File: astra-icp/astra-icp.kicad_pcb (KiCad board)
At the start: 2 copper layers, 127.5 x 97.5 mm, 45 parts, among them J1 Conn_02x05_Top_Bottom

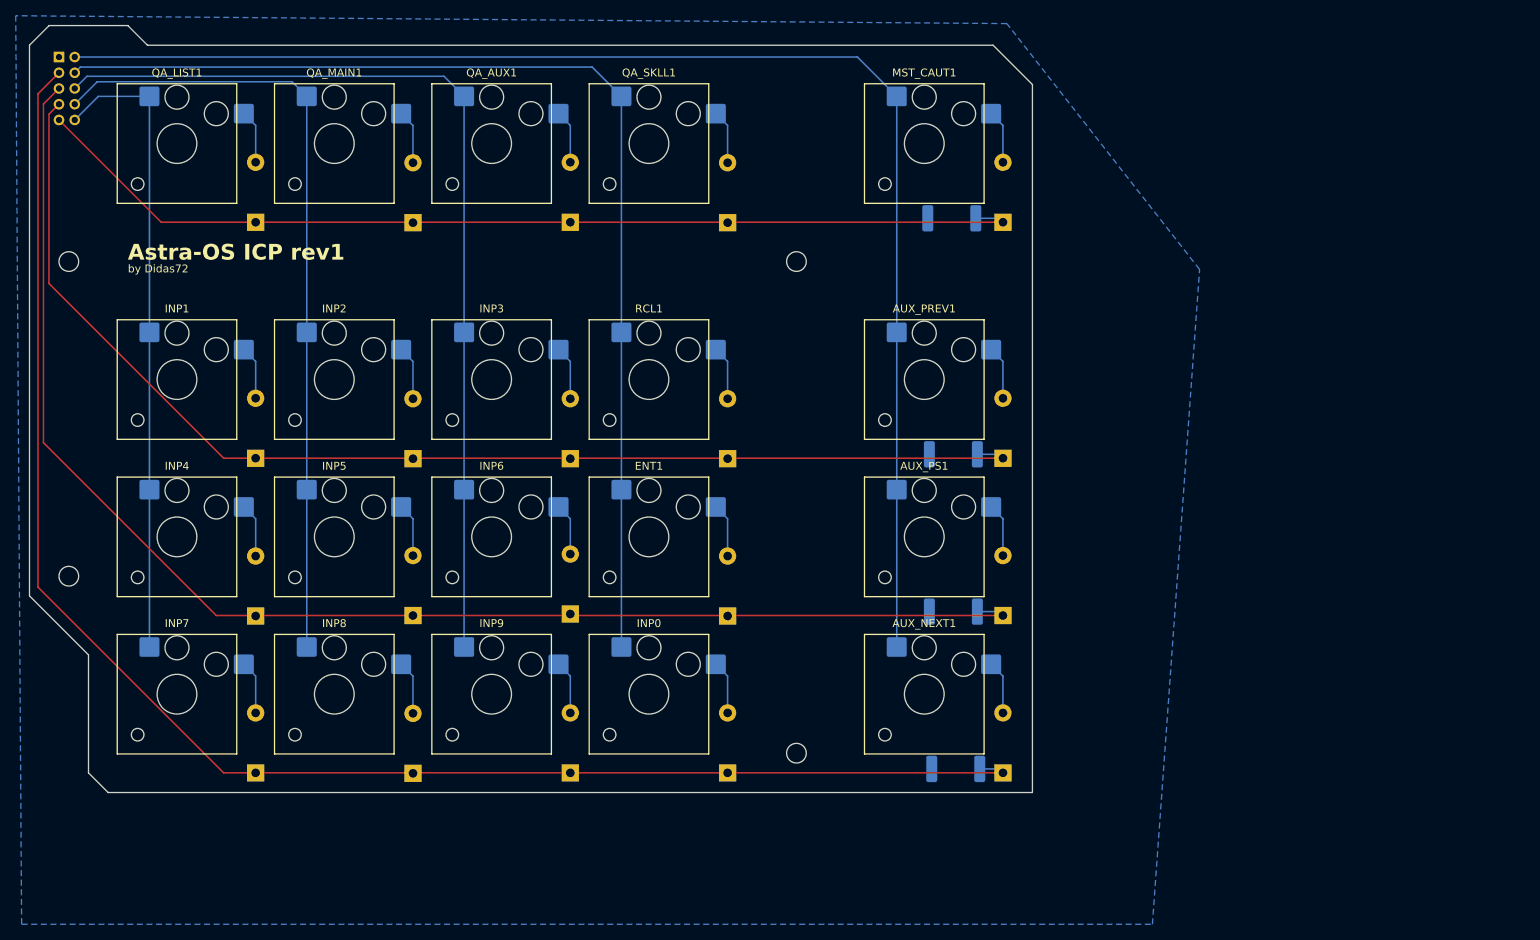
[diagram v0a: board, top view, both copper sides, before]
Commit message: feat: Schematic and partial PCB for ICP rev2
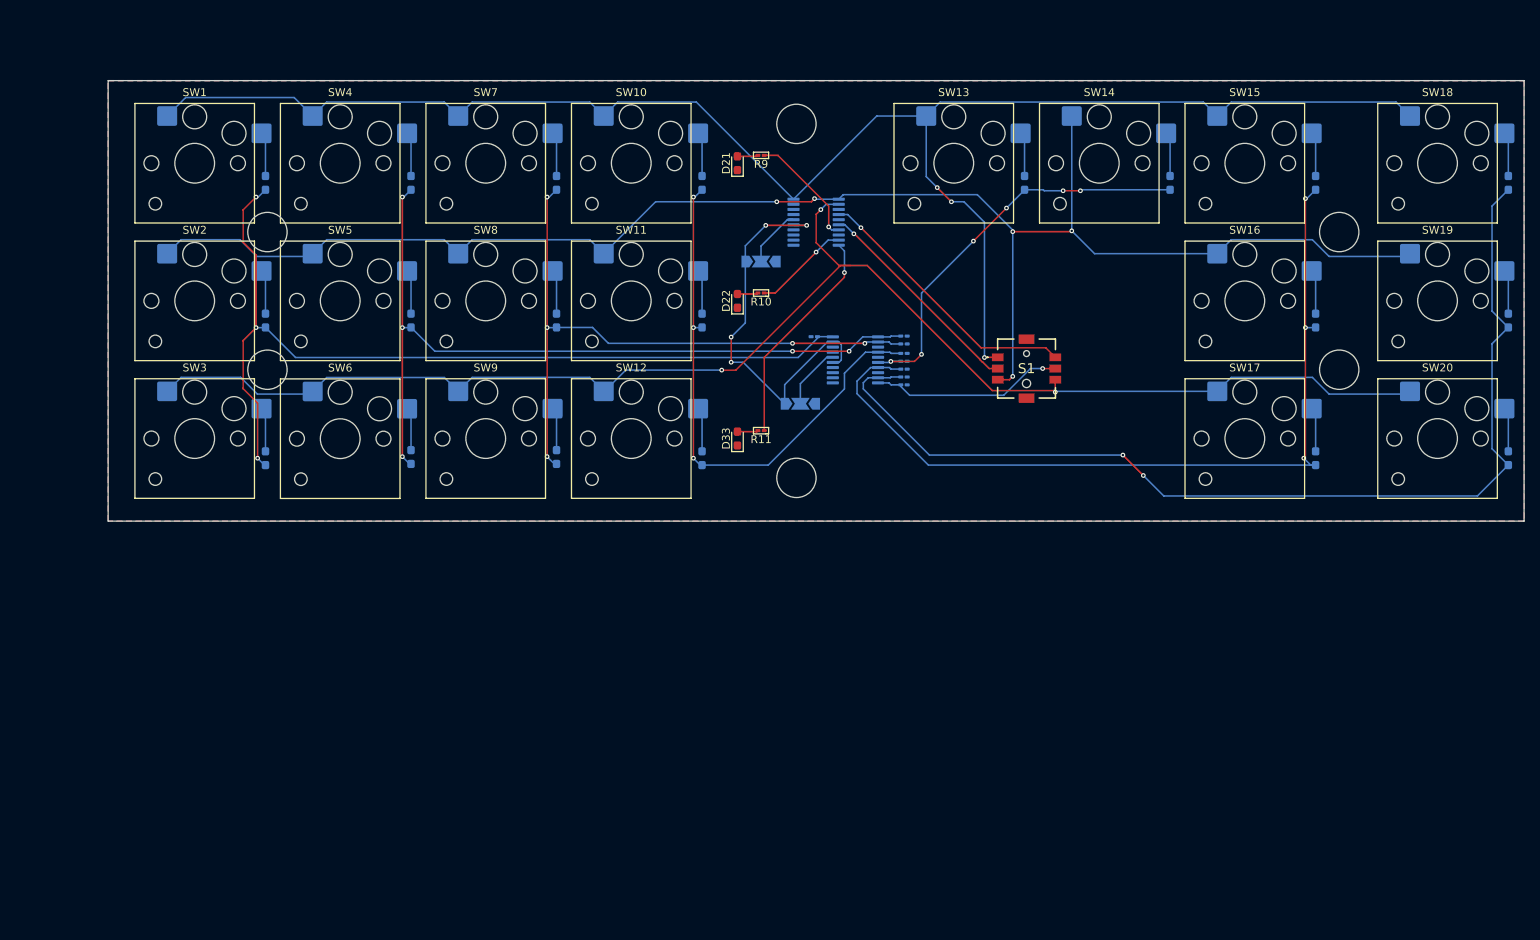
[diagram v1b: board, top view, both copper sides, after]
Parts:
- removed AUX_NEXT1, AUX_PREV1, AUX_PS1, ENT1, INP0, INP1, INP2, INP3, INP4, INP5, INP6, INP7, INP8, INP9, MST_CAUT1, QA_AUX1, QA_LIST1, QA_MAIN1, QA_SKLL1, RCL1: SW_Push_Dual, PCM_Switch_Keyboard_Hotswap_Kailh:SW_Hotswap_Kailh_Choc_V2_1.00u
- removed J1: Conn_02x05_Top_Bottom, Connector_PinSocket_2.00mm:PinSocket_2x05_P2.00mm_Vertical
- added D21: 599-2000-147F, LED_SMD:LED_0603_1608Metric_Pad1.05x0.95mm_HandSolder, F.Cu at (105.0, 32.5)
- added D22: 599-2000-147F, LED_SMD:LED_0603_1608Metric_Pad1.05x0.95mm_HandSolder, F.Cu at (105.0, 50.0)
- added D33: 599-2000-147F, LED_SMD:LED_0603_1608Metric_Pad1.05x0.95mm_HandSolder, F.Cu at (105.0, 67.5)
- added JP1: SolderJumper, Jumper:SolderJumper-3_P2.0mm_Open_TrianglePad1.0x1.5mm, B.Cu at (113.0, 63.1)
- added JP2: SolderJumper, Jumper:SolderJumper-3_P2.0mm_Open_TrianglePad1.0x1.5mm, B.Cu at (108.0, 45.0)
- added R10: 15, PCM_Resistor_SMD_AKL:R_0201_0603Metric_Pad0.64x0.40mm_HandSolder, F.Cu at (108.0, 49.0)
- added R11: 15, PCM_Resistor_SMD_AKL:R_0201_0603Metric_Pad0.64x0.40mm_HandSolder, F.Cu at (108.0, 66.5)
- added R5: 47k, PCM_Resistor_SMD_AKL:R_0201_0603Metric_Pad0.64x0.40mm_HandSolder, B.Cu at (126.2, 57.7)
- added R6: 47k, PCM_Resistor_SMD_AKL:R_0201_0603Metric_Pad0.64x0.40mm_HandSolder, B.Cu at (126.2, 58.7)
- added R7: 47k, PCM_Resistor_SMD_AKL:R_0201_0603Metric_Pad0.64x0.40mm_HandSolder, B.Cu at (126.2, 59.7)
- added R8: 47k, PCM_Resistor_SMD_AKL:R_0201_0603Metric_Pad0.64x0.40mm_HandSolder, B.Cu at (126.2, 60.7)
- added R9: 15, PCM_Resistor_SMD_AKL:R_0201_0603Metric_Pad0.64x0.40mm_HandSolder, F.Cu at (108.0, 31.5)
- added S1: MU-BUE70R, footprints:MUBUE70R, F.Cu at (141.8, 58.6)
- added SW1: CHOC_HS, PCM_Switch_Keyboard_Hotswap_Kailh:SW_Hotswap_Kailh_Choc_V1V2_1.00u, F.Cu at (36.0, 32.5)
- added SW10: CHOC_HS, PCM_Switch_Keyboard_Hotswap_Kailh:SW_Hotswap_Kailh_Choc_V1V2_1.00u, F.Cu at (91.5, 32.5)
- added SW11: CHOC_HS, PCM_Switch_Keyboard_Hotswap_Kailh:SW_Hotswap_Kailh_Choc_V1V2_1.00u, F.Cu at (91.5, 50.0)
- added SW12: CHOC_HS, PCM_Switch_Keyboard_Hotswap_Kailh:SW_Hotswap_Kailh_Choc_V1V2_1.00u, F.Cu at (91.5, 67.5)
- added SW13: CHOC_HS, PCM_Switch_Keyboard_Hotswap_Kailh:SW_Hotswap_Kailh_Choc_V1V2_1.00u, F.Cu at (132.5, 32.5)
- added SW14: CHOC_HS, PCM_Switch_Keyboard_Hotswap_Kailh:SW_Hotswap_Kailh_Choc_V1V2_1.00u, F.Cu at (151.0, 32.5)
- added SW15: CHOC_HS, PCM_Switch_Keyboard_Hotswap_Kailh:SW_Hotswap_Kailh_Choc_V1V2_1.00u, F.Cu at (169.5, 32.5)
- added SW16: CHOC_HS, PCM_Switch_Keyboard_Hotswap_Kailh:SW_Hotswap_Kailh_Choc_V1V2_1.00u, F.Cu at (169.5, 50.0)
- added SW17: CHOC_HS, PCM_Switch_Keyboard_Hotswap_Kailh:SW_Hotswap_Kailh_Choc_V1V2_1.00u, F.Cu at (169.5, 67.5)
- added SW18: CHOC_HS, PCM_Switch_Keyboard_Hotswap_Kailh:SW_Hotswap_Kailh_Choc_V1V2_1.00u, F.Cu at (194.0, 32.5)
- added SW19: CHOC_HS, PCM_Switch_Keyboard_Hotswap_Kailh:SW_Hotswap_Kailh_Choc_V1V2_1.00u, F.Cu at (194.0, 50.0)
- added SW2: CHOC_HS, PCM_Switch_Keyboard_Hotswap_Kailh:SW_Hotswap_Kailh_Choc_V1V2_1.00u, F.Cu at (36.0, 50.0)
- added SW20: CHOC_HS, PCM_Switch_Keyboard_Hotswap_Kailh:SW_Hotswap_Kailh_Choc_V1V2_1.00u, F.Cu at (194.0, 67.5)
- added SW3: CHOC_HS, PCM_Switch_Keyboard_Hotswap_Kailh:SW_Hotswap_Kailh_Choc_V1V2_1.00u, F.Cu at (36.0, 67.5)
- added SW4: CHOC_HS, PCM_Switch_Keyboard_Hotswap_Kailh:SW_Hotswap_Kailh_Choc_V1V2_1.00u, F.Cu at (54.5, 32.5)
- added SW5: CHOC_HS, PCM_Switch_Keyboard_Hotswap_Kailh:SW_Hotswap_Kailh_Choc_V1V2_1.00u, F.Cu at (54.5, 50.0)
- added SW6: CHOC_HS, PCM_Switch_Keyboard_Hotswap_Kailh:SW_Hotswap_Kailh_Choc_V1V2_1.00u, F.Cu at (54.5, 67.5)
- added SW7: CHOC_HS, PCM_Switch_Keyboard_Hotswap_Kailh:SW_Hotswap_Kailh_Choc_V1V2_1.00u, F.Cu at (73.0, 32.5)
- added SW8: CHOC_HS, PCM_Switch_Keyboard_Hotswap_Kailh:SW_Hotswap_Kailh_Choc_V1V2_1.00u, F.Cu at (73.0, 50.0)
- added SW9: CHOC_HS, PCM_Switch_Keyboard_Hotswap_Kailh:SW_Hotswap_Kailh_Choc_V1V2_1.00u, F.Cu at (73.0, 67.5)
- added U1: PCF8574ATS, Package_SO:SSOP-20_4.4x6.5mm_P0.65mm, B.Cu at (115.0, 40.0)
- added U2: PCF8574ATS, Package_SO:SSOP-20_4.4x6.5mm_P0.65mm, B.Cu at (120.0, 57.5)
- D1, D10, D11, D12, D13, D14, D15, D16, D17, D18, D19, D2, D20, D3, D4, D5, D6, D7, D8, D9: value 1N5400 -> D; footprint Diode_THT:D_DO-41_SOD81_P7.62mm_Horizontal -> PCM_Diode_SMD_AKL:D_0603_1608Metric_Pad1.05x0.95mm_HandSolder
- R1, R2, R3, R4: footprint Resistor_SMD:R_2512_6332Metric_Pad1.40x3.35mm_HandSolder -> PCM_Resistor_SMD_AKL:R_0201_0603Metric_Pad0.64x0.40mm_HandSolder
- moved D15 120.8 mm to (178.5, 35.0)
- moved D13 95.2 mm to (141.5, 35.0)
- moved D16 94.3 mm to (178.5, 52.5)
- moved D14 93.9 mm to (160.0, 35.0)
- moved D11 80.8 mm to (100.5, 52.5)
- moved D10 79.1 mm to (100.5, 35.0)
- moved D17 77.4 mm to (178.5, 70.0)
- moved D5 76.3 mm to (63.5, 52.5)
- moved D20 75.7 mm to (203.0, 70.0)
- moved D19 74.4 mm to (203.0, 52.5)
- moved D18 73.2 mm to (203.0, 35.0)
- moved R1 57.8 mm to (114.8, 54.5)
- moved D12 54.4 mm to (100.5, 70.0)
- moved D3 49.0 mm to (45.0, 70.0)
- moved D4 40.6 mm to (63.5, 35.0)
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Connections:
- D1 pad 1: Net-(D1-K) -> COL0
- D10 pad 1: Net-(D10-K) -> COL3
- D11 pad 1: Net-(D11-K) -> COL3
- D12 pad 1: Net-(D11-K) -> COL3
- D13 pad 1: Net-(D10-K) -> COL4
- D14 pad 1: Net-(D10-K) -> COL4
- D15 pad 1: Net-(D11-K) -> COL5
- D16 pad 1: Net-(D11-K) -> COL5
- D17 pad 1: Net-(D10-K) -> COL5
- D18 pad 1: Net-(D18-K) -> COL6
- D19 pad 1: Net-(D10-K) -> COL6
- D2 pad 1: Net-(D1-K) -> COL0
- D20 pad 1: Net-(D11-K) -> COL6
- D3 pad 1: Net-(D1-K) -> COL0
- D4 pad 1: Net-(D1-K) -> COL1
- D5 pad 1: Net-(D1-K) -> COL1
- D6 pad 1: Net-(D18-K) -> COL1
- D7 pad 1: Net-(D18-K) -> COL2
- D8 pad 1: Net-(D18-K) -> COL2
- D9 pad 1: Net-(D18-K) -> COL2
- R1 pad 2: Net-(D11-K) -> COL0
- R2 pad 2: Net-(D10-K) -> COL1
- R3 pad 2: Net-(D18-K) -> COL2
- R4 pad 2: Net-(D1-K) -> COL3
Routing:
- net ROW0: track 0.00 -> 212.5 mm, vias 0 -> 3
- net ROW1: track 0.00 -> 206.0 mm, vias 0 -> 5
- net Net-(D11-K): track 202.1 -> 0.00 mm
- net ROW2: track 0.00 -> 192.0 mm, vias 0 -> 3
- net Net-(D10-K): track 180.4 -> 0.00 mm
- net Net-(J1-Pin_2): track 176.6 -> 0.00 mm
- net Net-(D18-K): track 157.3 -> 0.00 mm
- net Net-(J1-Pin_4): track 141.3 -> 0.00 mm
- net COL6: track 0.00 -> 133.6 mm, vias 0 -> 2
- net Net-(D1-K): track 129.0 -> 0.00 mm
- net Net-(J1-Pin_6): track 121.2 -> 0.00 mm
- net COL0: track 0.00 -> 115.1 mm, vias 0 -> 3
- net COL5: track 0.00 -> 108.5 mm, vias 0 -> 3
- net Net-(J1-Pin_8): track 101.4 -> 0.00 mm
- net COL1: track 0.00 -> 101.4 mm, vias 0 -> 5
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- added copper zone on F.Cu, net GND
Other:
- board size 127.5 x 97.5 mm -> 180 x 56 mm
- board text removed: "Astra-OS ICP rev1"
- board text removed: "by Didas72"

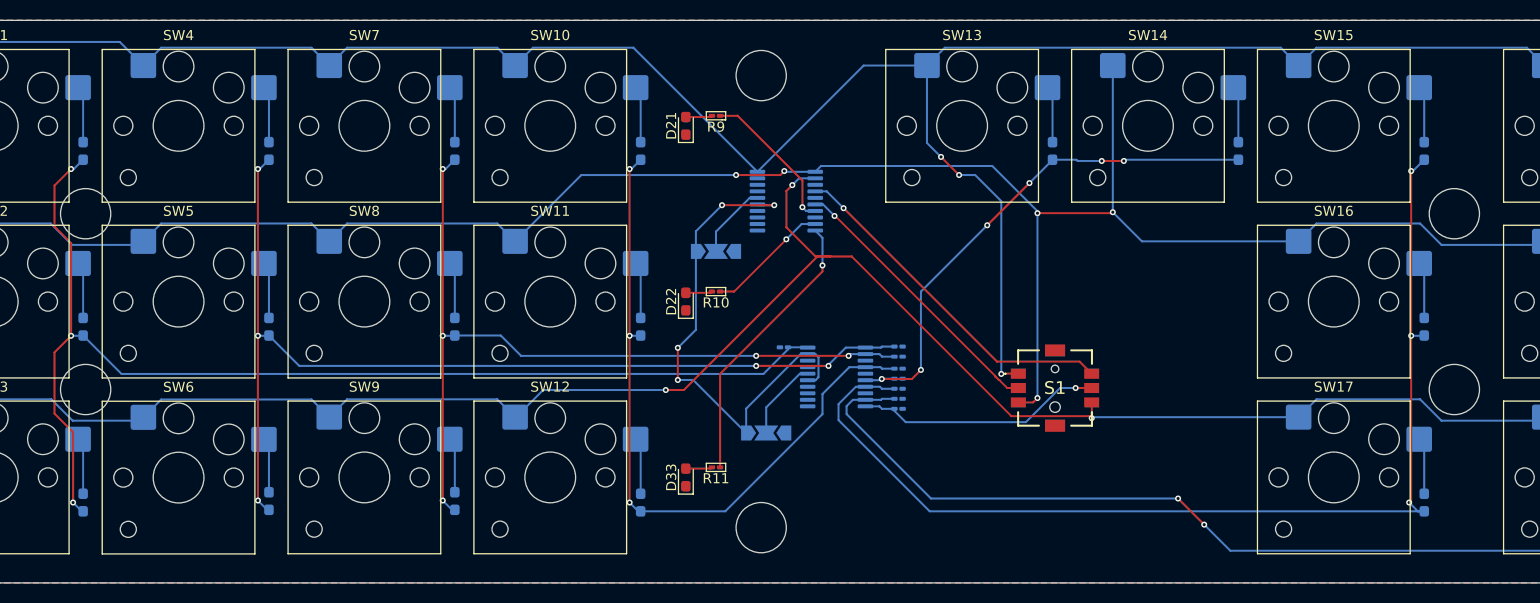
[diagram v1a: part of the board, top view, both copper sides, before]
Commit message: feat: Work on connectors and MCU-CAN signaling
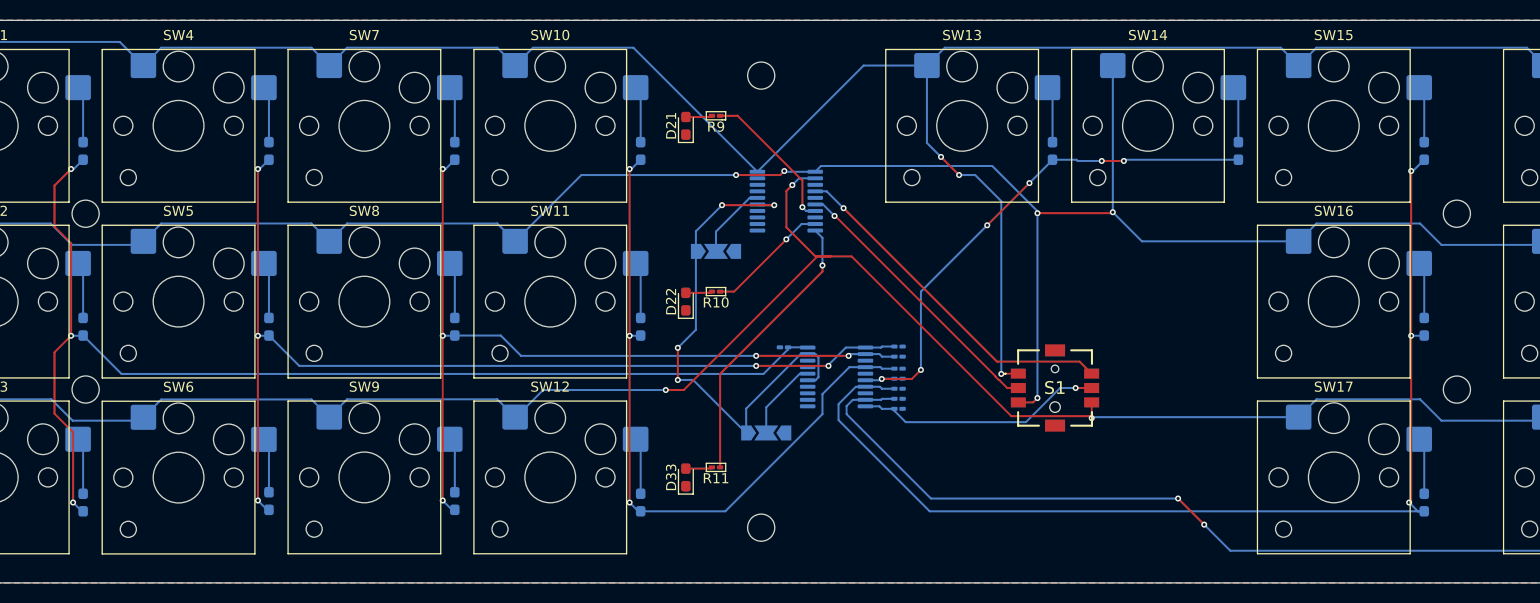
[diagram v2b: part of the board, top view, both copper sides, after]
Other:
- outline, holes or cut-outs redrawn
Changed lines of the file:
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@@
 	)
 	(gr_circle
-		(center 45.25 41.25)
-		(end 47.75 41.25)
-		(stroke
-			(width 0.05)
-			(type default)
-		)
-		(fill no)
-		(layer "Edge.Cuts")
-	)
-	(gr_circle
-		(center 181.5 41.25)
-		(end 184 41.25)
+		(center 181.752858 58.755315)
+		(end 183.102858 58.755315)
 		(stroke
 			(width 0.05)
@@
 	)
 	(gr_circle
-		(center 181.5 58.75)
-		(end 184 58.75)
+		(center 181.75 41.25)
+		(end 183.1 41.25)
+		(stroke
+			(width 0.05)
+			(type default)
+		)
+		(fill no)
+		(layer "Edge.Cuts")
+	)
+	(gr_circle
+		(center 112.5 72.5)
+		(end 113.85 72.5)
+		(stroke
+			(width 0.05)
+			(type default)
+		)
+		(fill no)
+		(layer "Edge.Cuts")
+	)
+	(gr_circle
+		(center 45.25 41.25)
+		(end 46.6 41.25)
+		(stroke
+			(width 0.05)
+			(type default)
+		)
+		(fill no)
+		(layer "Edge.Cuts")
+	)
+	(gr_circle
+		(center 45.25 58.75)
+		(end 46.6 58.75)
 		(stroke
 			(width 0.05)
@@
 	(gr_circle
 		(center 112.5 27.5)
-		(end 115 27.5)
+		(end 113.85 27.5)
 		(stroke
 			(width 0.05)
-			(type default)
-		)
-		(fill no)
-		(layer "Edge.Cuts")
-	)
-	(gr_circle
-		(center 112.5 72.5)
-		(end 115 72.5)
-		(stroke
-			(width 0.05)
-			(type default)
-		)
-		(fill no)
-		(layer "Edge.Cuts")
-	)
-	(gr_circle
-		(center 45.25 58.75)
-		(end 47.75 58.75)
-		(stroke
-			(width 0.05)

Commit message: feat: Mostly done ICP PCB
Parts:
- removed JP1, JP2: SolderJumper, Jumper:SolderJumper-3_P2.0mm_Open_TrianglePad1.0x1.5mm
- removed U1, U2: PCF8574ATS, Package_SO:SSOP-20_4.4x6.5mm_P0.65mm
- added C1: 100n, Capacitor_SMD:C_0603_1608Metric_Pad1.08x0.95mm_HandSolder, B.Cu at (124.5, 56.0)
- added C2: 100n, Capacitor_SMD:C_0603_1608Metric_Pad1.08x0.95mm_HandSolder, B.Cu at (127.5, 63.5)
- added C3: 100n, Capacitor_SMD:C_0603_1608Metric_Pad1.08x0.95mm_HandSolder, B.Cu at (119.8, 40.2)
- added C4: 100n, Capacitor_SMD:C_0603_1608Metric_Pad1.08x0.95mm_HandSolder, B.Cu at (111.2, 51.2)
- added C5: 4.7p, Capacitor_SMD:C_0603_1608Metric_Pad1.08x0.95mm_HandSolder, B.Cu at (110.8, 40.2)
- added D23: 5V_IND, LED_SMD:LED_0603_1608Metric_Pad1.05x0.95mm_HandSolder, B.Cu at (132.8, 71.0)
- added D24: 3V3_IND, LED_SMD:LED_0603_1608Metric_Pad1.05x0.95mm_HandSolder, B.Cu at (132.8, 72.8)
- added IC1: ATA6561-GAQW-N, footprints:SOIC127P600X175-8N, B.Cu at (123.0, 60.8)
- added J1: PINHD_1x5_Male, Connector_PinHeader_2.54mm:PinHeader_1x05_P2.54mm_Vertical, B.Cu at (109.0, 35.2)
- added J2: PWR_IN, TerminalBlock_Phoenix:TerminalBlock_Phoenix_PT-1,5-3-5.0-H_1x03_P5.00mm_Horizontal, B.Cu at (154.0, 70.6)
- added J3: CAN_TERMINAL, TerminalBlock_Phoenix:TerminalBlock_Phoenix_PT-1,5-2-5.0-H_1x02_P5.00mm_Horizontal, B.Cu at (125.5, 71.1)
- added R12: 120, PCM_Resistor_SMD_AKL:R_0603_1608Metric_Pad1.05x0.95mm_HandSolder, B.Cu at (123.0, 65.2)
- added R13: 145, PCM_Resistor_SMD_AKL:R_0603_1608Metric_Pad1.05x0.95mm_HandSolder, B.Cu at (137.2, 71.0)
- added R14: 60.4, PCM_Resistor_SMD_AKL:R_0603_1608Metric_Pad1.05x0.95mm_HandSolder, B.Cu at (137.2, 72.8)
- added U3: STM32F042C4Tx, Package_QFP:LQFP-48_7x7mm_P0.5mm, B.Cu at (115.2, 45.8)
- D21: value 599-2000-147F -> NUM
- D22: value 599-2000-147F -> ANF
- D33: value 599-2000-147F -> ALP
- moved R4 20.2 mm to (109.5, 45.2), turned to -90 degrees
- moved R3 19.5 mm to (108.2, 47.8), turned to 0 degrees
- moved R2 17.6 mm to (109.5, 48.8), turned to 90 degrees
- moved R5 12.0 mm to (121.8, 46.5), turned to -90 degrees
- moved R7 11.8 mm to (120.2, 49.5), turned to 0 degrees
- moved R8 11.7 mm to (119.5, 51.0)
- moved R6 11.4 mm to (122.2, 48.0)
- moved R1 6.50 mm to (109.5, 50.8), turned to 90 degrees
- moved R10 2.92 mm to (105.5, 47.5)
- moved R11 2.92 mm to (105.5, 65.0)
- moved R9 2.92 mm to (105.5, 30.0)
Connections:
- S1 pad A1: ROW0 -> ROW5
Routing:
- net +3V3: track 50.3 -> 110.8 mm, vias 4 -> 2
- net +5V: track 0.00 -> 34.5 mm, vias 0 -> 1
- net ROW0: track 212.5 -> 181.9 mm, vias 3 -> 0
- net CAN_RX: track 0.00 -> 26.0 mm, vias 0 -> 2
- net ROW5: track 0.00 -> 25.1 mm, vias 0 -> 1
- net STBY: track 0.00 -> 23.2 mm, vias 0 -> 2
- net CAN_TX: track 0.00 -> 20.0 mm, vias 0 -> 2
- net COL3: track 69.7 -> 52.6 mm
- net SWDIO: track 0.00 -> 13.6 mm, vias 0 -> 1
- net NRST: track 0.00 -> 12.9 mm, vias 0 -> 1
- net COL1: track 101.4 -> 90.1 mm, vias 5 -> 3
- net COL2: track 82.2 -> 71.8 mm, vias 5 -> 3
- net ROW1: track 206.0 -> 216.1 mm, vias 5 -> 7
- net COL5: track 108.5 -> 98.6 mm
- net LD_ALP: track 28.1 -> 18.2 mm
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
